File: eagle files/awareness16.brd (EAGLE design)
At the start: 77.2 x 102.2 mm, 91 parts, among them J1 TYPE-C-31-M-12, Q1 16MHz

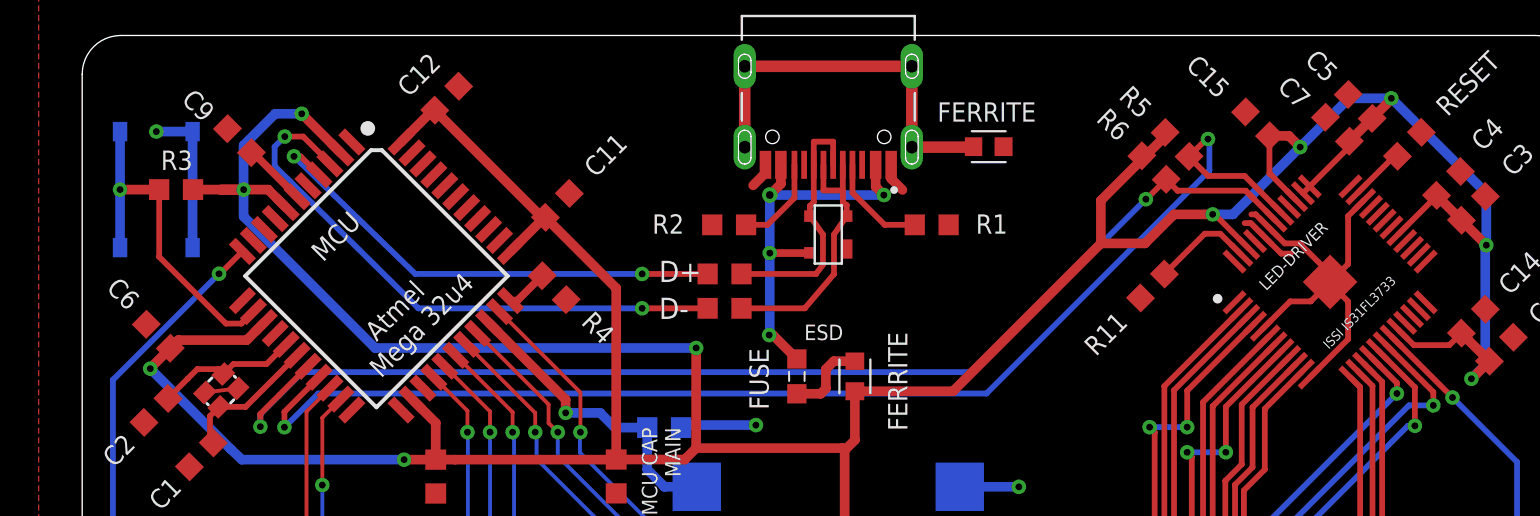
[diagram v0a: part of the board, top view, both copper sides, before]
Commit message: Repo clean up, readme update
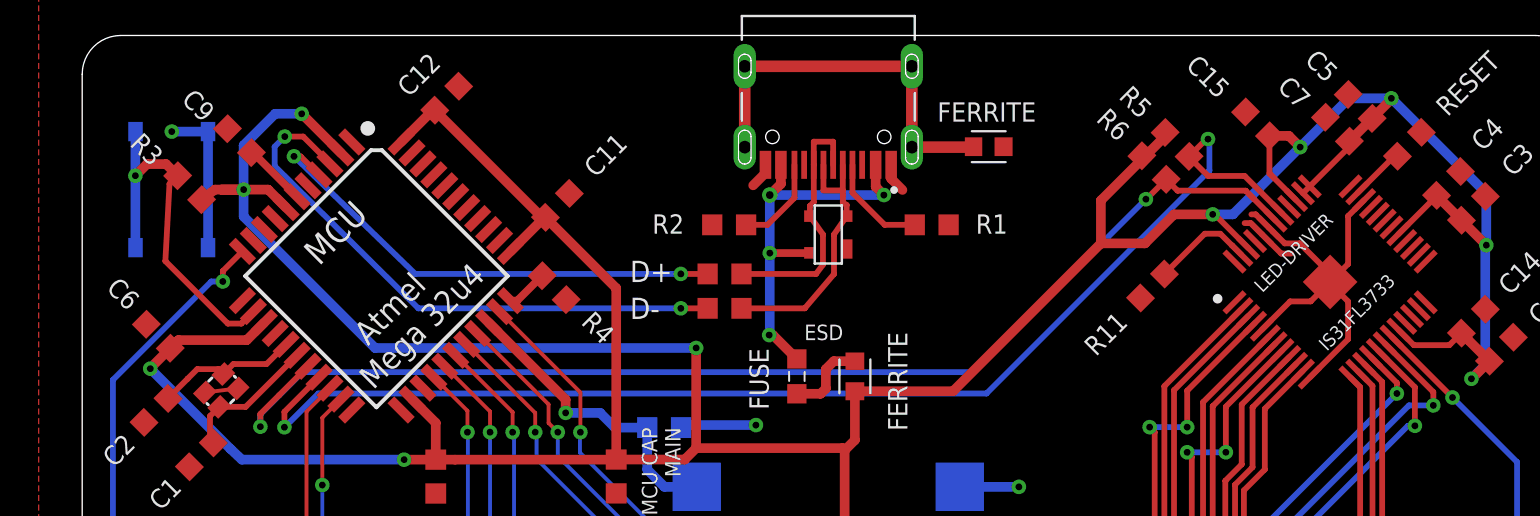
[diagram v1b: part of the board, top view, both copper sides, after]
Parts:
- moved S1 0.80 mm to (13.7, 103.3)
- moved R3 0.71 mm to (14.6, 103.4), turned to 135 degrees
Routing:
- net N$17: track 18.1 -> 19.4 mm
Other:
- board text added: "IS31FL3733"
- board text removed: "ISSI IS31FL3733"

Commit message: Minor board adjustments
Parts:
- moved R2 0.24 mm to (42.3, 101.5)
